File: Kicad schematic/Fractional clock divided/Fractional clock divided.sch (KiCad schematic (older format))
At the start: 51 parts, among them Q1 2N3904, Q2 2N3904, Q3 2N3904, Q4 2N3904, SW1 SPDT on-on, SW2 SPDT on-off-on, SW3 SPDT on-on, SW4 Rotary_Encoder_Switch, U1 TL074, U2 Teensy-LC

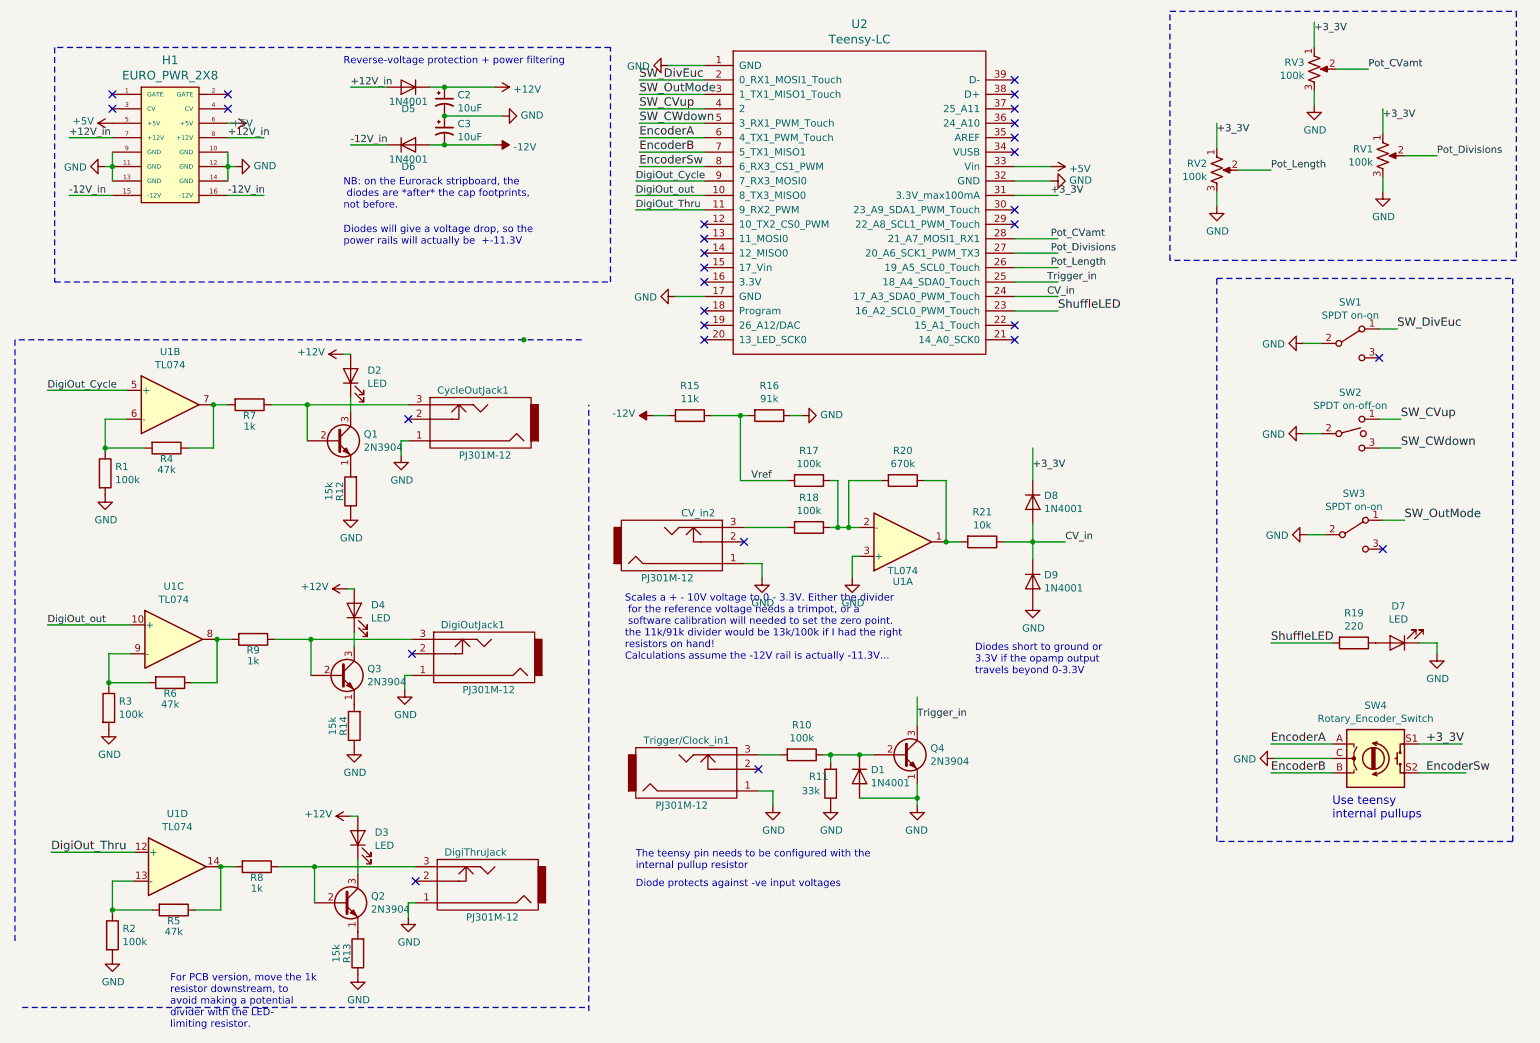
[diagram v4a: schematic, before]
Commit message: circuit bugfixes
Circuit bugfixes:
Added pulldown resistor to the encoder switch

Changed feedback resistor on the input CV opamp, to keep it within the correct voltage range. My choice (15k) was probably a little conservative - on testing, the voltage seen by the teensy can't go above 2.2V now. Stick with it for now though.
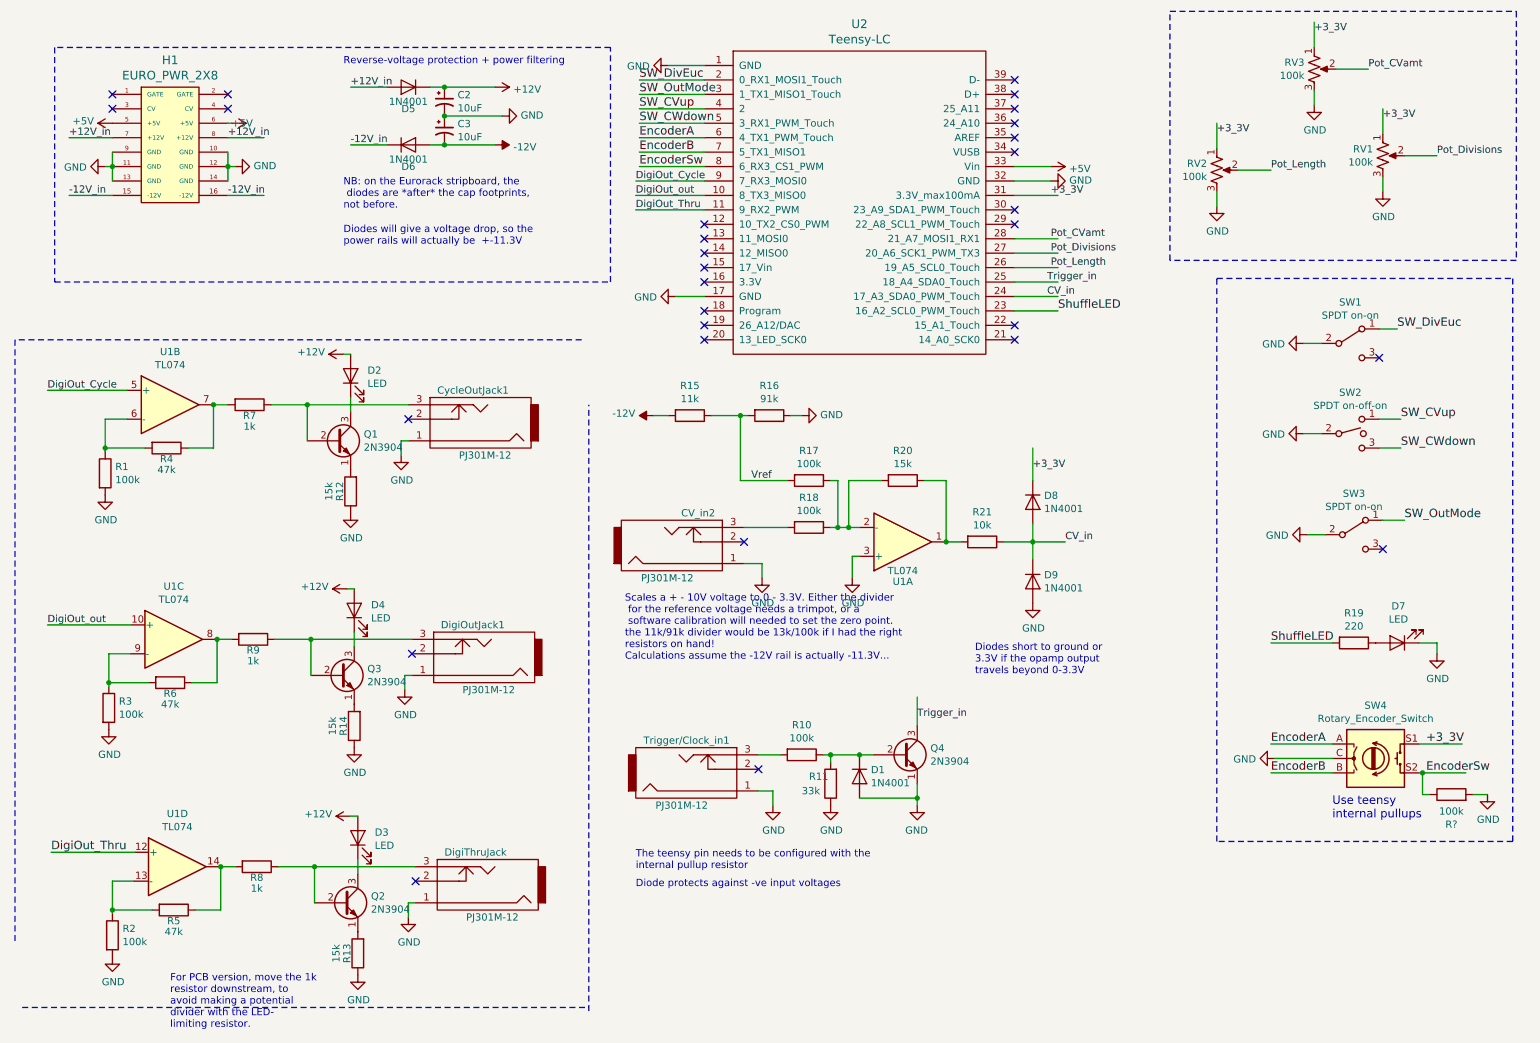
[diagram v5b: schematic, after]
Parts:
- added R?: 100k, symbol Device:R
- R20: value 670k -> 15k
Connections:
- wire segments 145 -> 149
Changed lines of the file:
@@
 P 6875 3825
 F 0 "R20" V 6668 3825 50  0000 C CNN
-F 1 "670k" V 6759 3825 50  0000 C CNN
+F 1 "15k" V 6759 3825 50  0000 C CNN
 F 2 "" V 6805 3825 50  0001 C CNN
 F 3 "~" H 6875 3825 50  0001 C CNN
@@
 Wire Wire Line
 	10450 5650 10750 5650
-Wire Wire Line
-	10450 5850 10775 5850
 Wire Wire Line
 	5500 1050 5050 1050
@@
 Wire Notes Line
 	11125 2300 8725 2300
-Connection ~ 4250 2850
 Text Notes 1800 7625 0    50   ~ 0
 For PCB version, move the 1k\nresistor downstream, to \navoid making a potential \ndivider with the LED-\nlimiting resistor.
+$Comp
+L Device:R R?
+U 1 1 5BE8D16E
+P 10675 6000
+F 0 "R?" V 10468 6000 50  0000 C CNN
+F 1 "100k" V 10559 6000 50  0000 C CNN
+F 2 "" V 10605 6000 50  0001 C CNN
+F 3 "~" H 10675 6000 50  0001 C CNN
+	1    10675 6000
+	0    -1   -1   0
+$EndComp
+$Comp
+L power:GND #PWR?
+U 1 1 5BE8D2E2
+P 10925 6000
+F 0 "#PWR?" H 10925 5750 50  0001 C CNN
+F 1 "GND" H 10930 5827 50  0000 C CNN
+F 2 "" H 10925 6000 50  0001 C CNN
+F 3 "" H 10925 6000 50  0001 C CNN
+	1    10925 6000
+	1    0    0    -1
+$EndComp
+Wire Wire Line
+	10450 5850 10475 5850
+Wire Wire Line
+	10825 6000 10925 6000
+Wire Wire Line
+	10525 6000 10475 6000
+Wire Wire Line
+	10475 6000 10475 5850
+Connection ~ 10475 5850
+Wire Wire Line
+	10475 5850 10775 5850
 $EndSCHEMATC

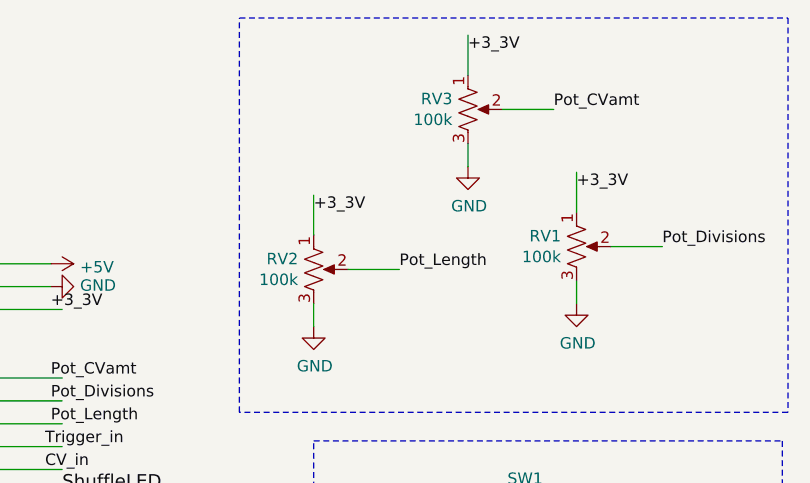
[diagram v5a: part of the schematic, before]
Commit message: Updated pot values for faster readings
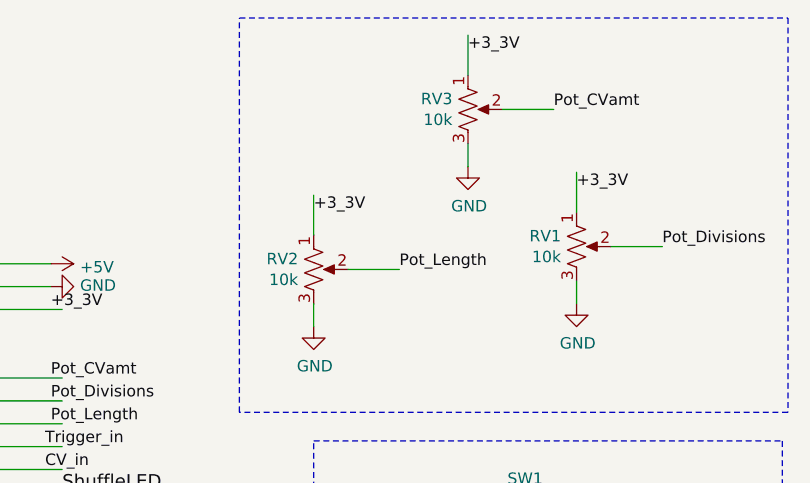
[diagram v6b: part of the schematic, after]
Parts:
- RV1, RV2, RV3: value 100k -> 10k
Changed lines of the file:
@@
 P 10200 1575
 F 0 "RV1" H 10132 1621 50  0000 R CNN
-F 1 "100k" H 10132 1530 50  0000 R CNN
+F 1 "10k" H 10132 1530 50  0000 R CNN
 F 2 "" H 10200 1575 50  0001 C CNN
 F 3 "~" H 10200 1575 50  0001 C CNN
@@
 P 9050 1675
 F 0 "RV2" H 8982 1721 50  0000 R CNN
-F 1 "100k" H 8982 1630 50  0000 R CNN
+F 1 "10k" H 8982 1630 50  0000 R CNN
 F 2 "" H 9050 1675 50  0001 C CNN
 F 3 "~" H 9050 1675 50  0001 C CNN
@@
 P 9725 975
 F 0 "RV3" H 9657 1021 50  0000 R CNN
-F 1 "100k" H 9657 930 50  0000 R CNN
+F 1 "10k" H 9657 930 50  0000 R CNN
 F 2 "" H 9725 975 50  0001 C CNN
 F 3 "~" H 9725 975 50  0001 C CNN
